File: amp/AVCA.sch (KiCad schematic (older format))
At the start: 19 parts

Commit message: reworked amp sheets and notes
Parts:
- C1: renamed from C?; footprint (none) -> KiCad/Capacitors_ThroughHole.pretty:CP_Radial_D4.0mm_P2.00mm
- C2: renamed from C?; footprint (none) -> KiCad/Capacitors_ThroughHole.pretty:CP_Radial_D6.3mm_P2.50mm
- R10, R11, R12, R13, R5, R6, R7, R8, R9: renamed from R?; footprint (none) -> KiCad/Resistors_ThroughHole.pretty:R_Axial_DIN0204_L3.6mm_D1.6mm_P1.90mm_Vertical
- U1: renamed from U?; footprint (none) -> KiCad/Housings_DIP.pretty:DIP-14_W7.62mm
- U3: renamed from U?; footprint (none) -> KiCad/Housings_DIP.pretty:DIP-16_W7.62mm
- gave numbers to parts that had none: 2
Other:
- note added: "0.5*VIN/VT*IABC=IOUT\nVIN=5V,IABC=1mA -> IOUT= .385mA\n13K converts back to 5V output"
- note removed: "A-VCA"
- moved on the sheet: R10, R5, R8, U1A, U3A

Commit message: update amp config for quad-cascade design
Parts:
- removed C2: 1u, KiCad/Capacitors_ThroughHole.pretty:CP_Radial_D6.3mm_P2.50mm, symbol Device:C
- removed R13: R, KiCad/Resistors_ThroughHole.pretty:R_Axial_DIN0204_L3.6mm_D1.6mm_P1.90mm_Vertical, symbol Device:R
- removed RV5: MASTER_VOL_A_10K, symbol Device:R_POT_Dual_Separate
- removed unit 2 of U3
- added RV?: 100K, symbol Device:R_POT
- renumbered C1 to C?, Q1 to Q?, R11 to R?, R12 to R?, R9 to R?, R6 to R?, R7 to R?, R5 to R?, R8 to R?, R10 to R?, U1 to U?, U3 to U?
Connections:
- wire segments 64 -> 58
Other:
- note added: "Subtract 0-5V from CV, providing offset control.\nThis isn’t perfectly linear but it’s close enough"
- note removed: "Subtract 5V from CV"
- moved on the sheet: R?

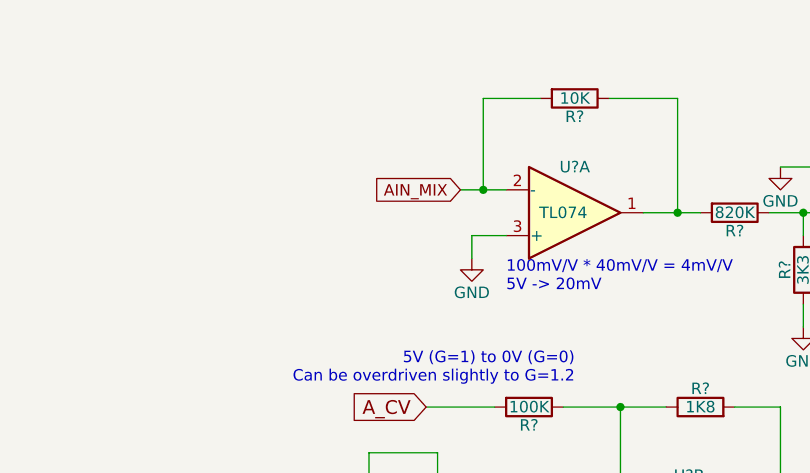
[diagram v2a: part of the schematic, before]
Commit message: add eurorack connector, fix some issues
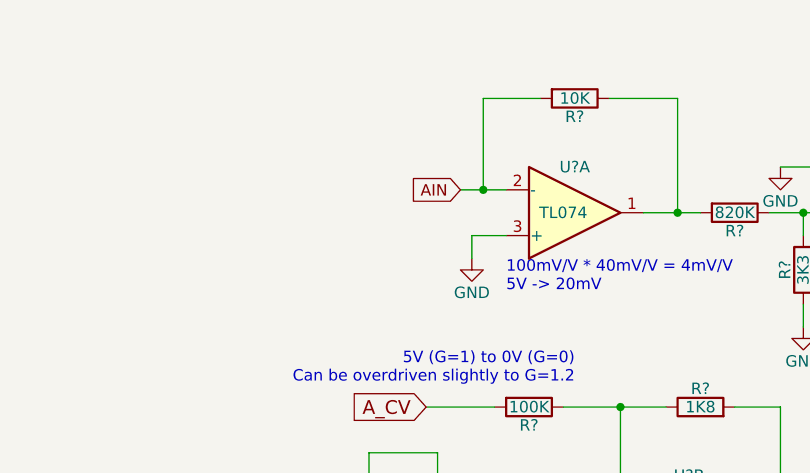
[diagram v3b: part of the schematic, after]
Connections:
- net AIN_MIX renamed AIN
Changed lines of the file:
@@
 100mV/V * 40mV/V = 4mV/V\n5V -> 20mV
 Text GLabel 3700 2600 0    50   Input ~ 0
-AIN_MIX
+AIN
 Wire Wire Line
 	3700 2600 3800 2600
